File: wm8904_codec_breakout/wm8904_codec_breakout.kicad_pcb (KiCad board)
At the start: 2 copper layers, 40 x 40 mm, 30 parts, among them J101 Conn_01x12_Female, J102 Conn_01x12_Female, J103 AudioJack3, J104 AudioJack3, U101 AMS1117-1.8, U201 wm8904

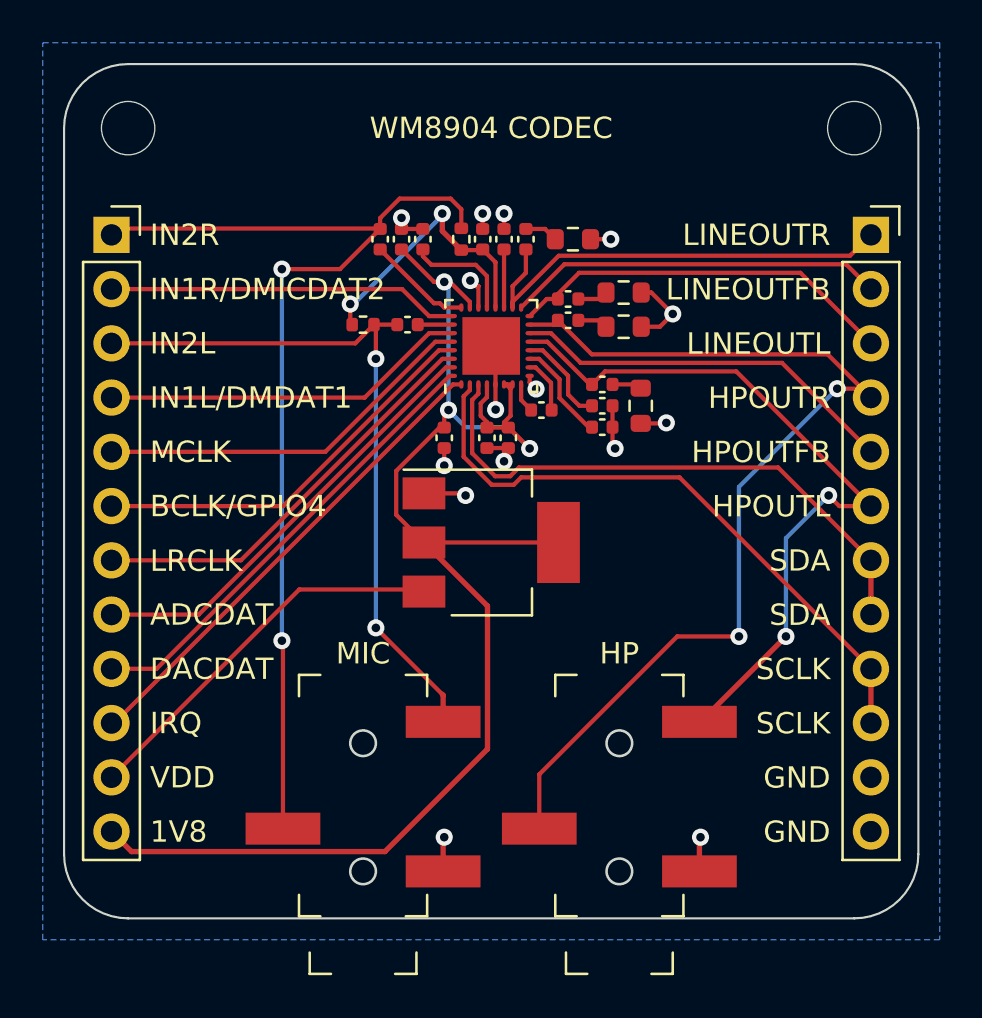
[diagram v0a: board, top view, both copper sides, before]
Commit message: [wm8904_codec_breakout] connect LINEOUTFB and HPOUTFB to ground and bump board version to v2
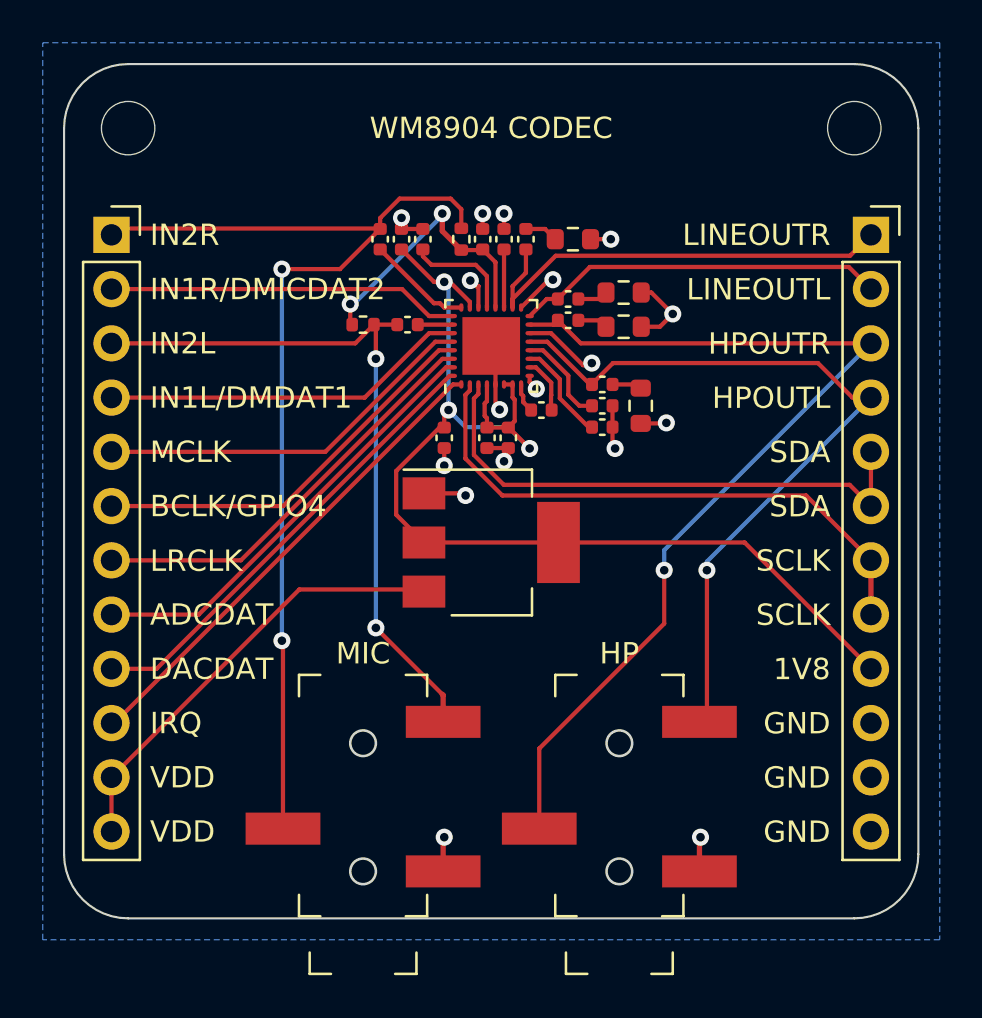
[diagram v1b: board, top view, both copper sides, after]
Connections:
- J101 pad 12: 1V8 -> VDD
- J102 pad 10: SCLK -> GND
- J102 pad 2: LINEOUTFB -> LINEOUTL
- J102 pad 3: LINEOUTL -> HPOUTR
- J102 pad 4: HPOUTR -> HPOUTL
- J102 pad 5: HPOUTFB -> SDA
- J102 pad 6: HPOUTL -> SDA
- J102 pad 7: SDA -> SCLK
- J102 pad 8: SDA -> SCLK
- J102 pad 9: SCLK -> 1V8
- U201 pad 14: HPOUTFB -> GND
- U201 pad 17: LINEOUTFB -> GND
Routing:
- net HPOUTFB: track 18.3 -> 0.00 mm
- net LINEOUTFB: track 17.7 -> 0.00 mm
- net 1V8: track 67.7 -> 53.5 mm
- net GND: track 24.0 -> 29.7 mm, vias 15 -> 17
- net VDD: track 18.3 -> 20.9 mm
- net SCLK: track 29.5 -> 27.1 mm
- net HPOUTR: track 47.5 -> 45.7 mm, vias 2 -> 1
- net SDA: track 27.0 -> 25.5 mm
- net HPOUTL: track 35.0 -> 36.4 mm, vias 2 -> 1
- net LINEOUTL: track 18.3 -> 17.4 mm
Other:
- board text added: "V2"
- board text removed: "HPOUTFB"
- board text removed: "LINEOUTFB"
- board text removed: "V1"

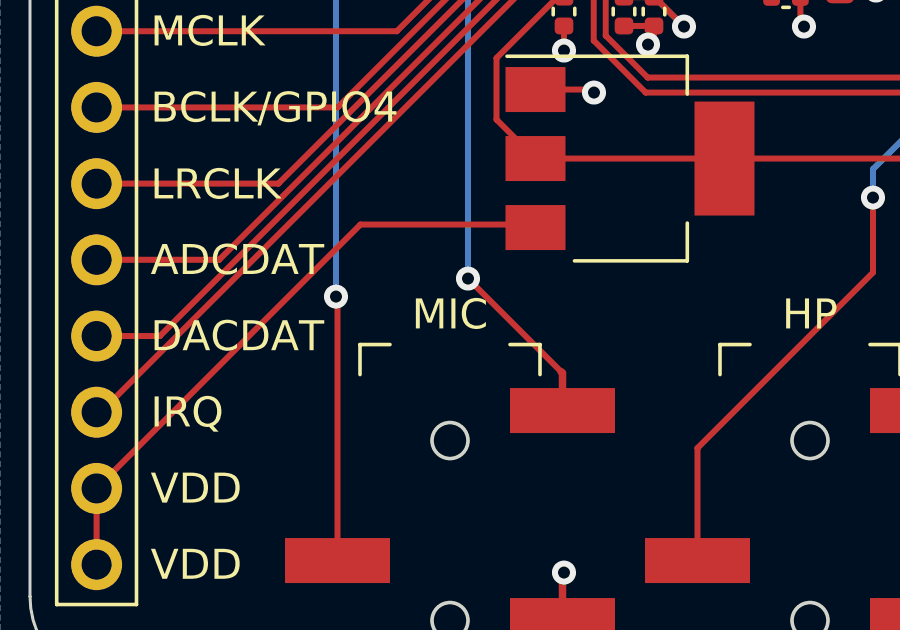
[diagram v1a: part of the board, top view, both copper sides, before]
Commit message: [wm8904_codec_breakout] Add v2 fabrication files
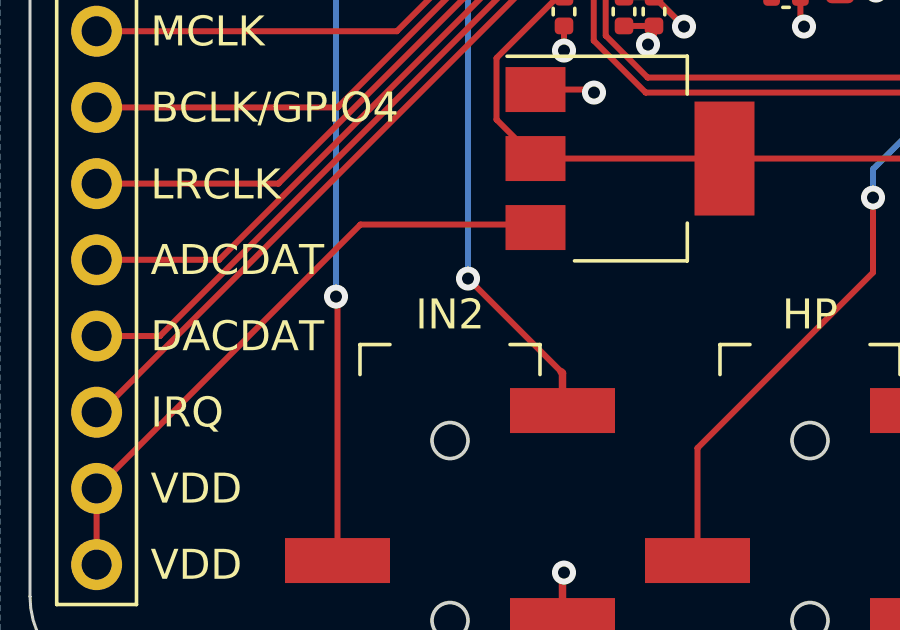
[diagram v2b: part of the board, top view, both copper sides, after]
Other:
- board text added: "IN2"
- board text removed: "MIC"
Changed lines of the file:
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@@
       (layerselection 0x00010fc_ffffffff)
       (disableapertmacros false)
-      (usegerberextensions false)
+      (usegerberextensions true)
       (usegerberattributes true)
-      (usegerberadvancedattributes true)
-      (creategerberjobfile true)
+      (usegerberadvancedattributes false)
+      (creategerberjobfile false)
       (svguseinch false)
       (svgprecision 6)
@@
       (plotinvisibletext false)
       (sketchpadsonfab false)
-      (subtractmaskfromsilk false)
+      (subtractmaskfromsilk true)
       (outputformat 1)
       (mirror false)
       (drillshape 0)
       (scaleselection 1)
-      (outputdirectory "fab/v1/jlcpcb")
+      (outputdirectory "fab/v2/jlcpcb")
     )
   )
@@
     (effects (font (size 1 1) (thickness 0.15)) (justify right))
   )
-  (gr_text "MIC" (at 144 87.6) (layer "F.SilkS")
+  (gr_text "IN2" (at 144 87.6) (layer "F.SilkS")
     (effects (font (size 1 1) (thickness 0.15)))
   )

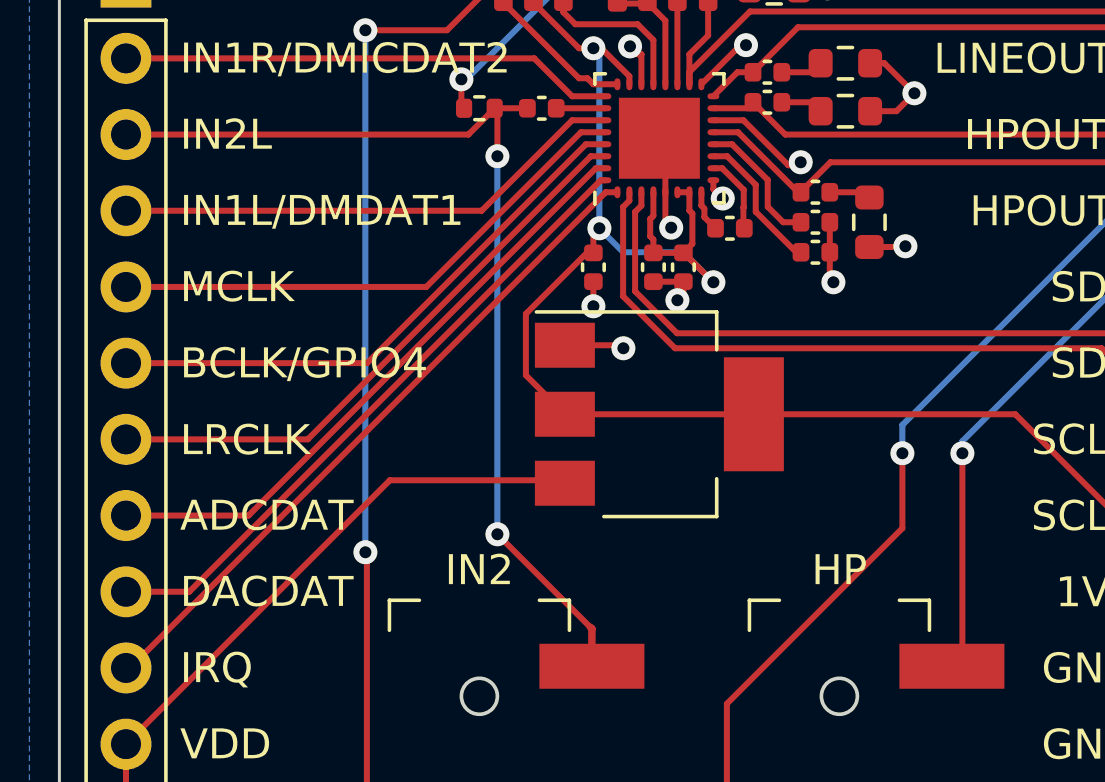
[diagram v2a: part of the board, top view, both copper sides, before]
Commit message: [wm8904_codec_breakout] Silkscreen label fixes
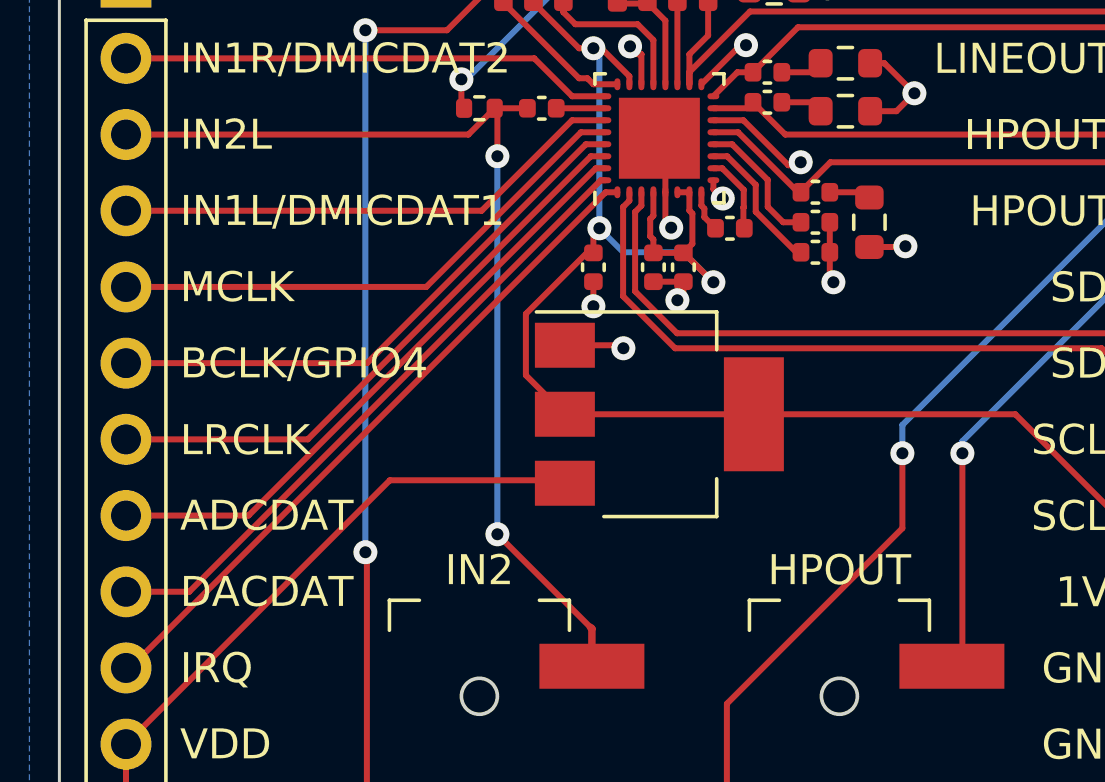
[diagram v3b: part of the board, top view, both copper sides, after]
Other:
- board text added: "HPOUT"
- board text added: "IN1L/DMICDAT1"
- board text removed: "HP"
- board text removed: "IN1L/DMDAT1"
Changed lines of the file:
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@@
     (effects (font (size 1 1) (thickness 0.15)) (justify left))
   )
-  (gr_text "IN1L/DMDAT1" (at 134.02 75.626) (layer "F.SilkS")
+  (gr_text "IN1L/DMICDAT1" (at 134.02 75.626) (layer "F.SilkS")
     (effects (font (size 1 1) (thickness 0.15)) (justify left))
   )
@@
     (effects (font (size 1 1) (thickness 0.15)) (justify left))
   )
-  (gr_text "HP" (at 156 87.6) (layer "F.SilkS")
+  (gr_text "HPOUT" (at 156 87.6) (layer "F.SilkS")
     (effects (font (size 1 1) (thickness 0.15)))
   )
